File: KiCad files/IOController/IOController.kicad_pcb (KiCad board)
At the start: 2 copper layers, 30 x 74.3 mm, 48 parts, among them IC1 TPS922054DMTR, J1 AVR-ISP-6, J2 XT60 Horizontal Socket, J3 edge connector, Q1 BSS138, SW1 RotaryEncoder_Switch, SW2 TL3342, U1 LP2985-1.8, U3 LP2985-5.0, U4 ATtiny45V-10X

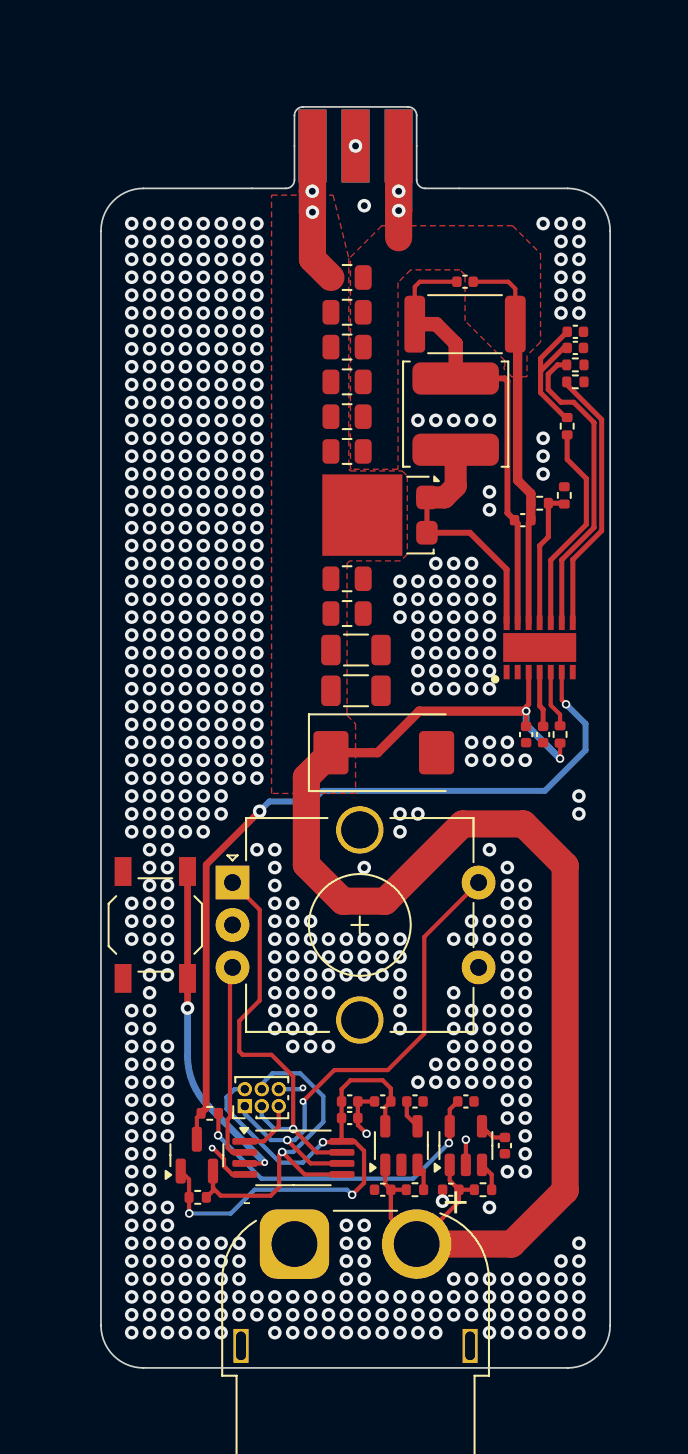
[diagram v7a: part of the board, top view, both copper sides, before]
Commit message: small adjustment to zones and added stitching vias
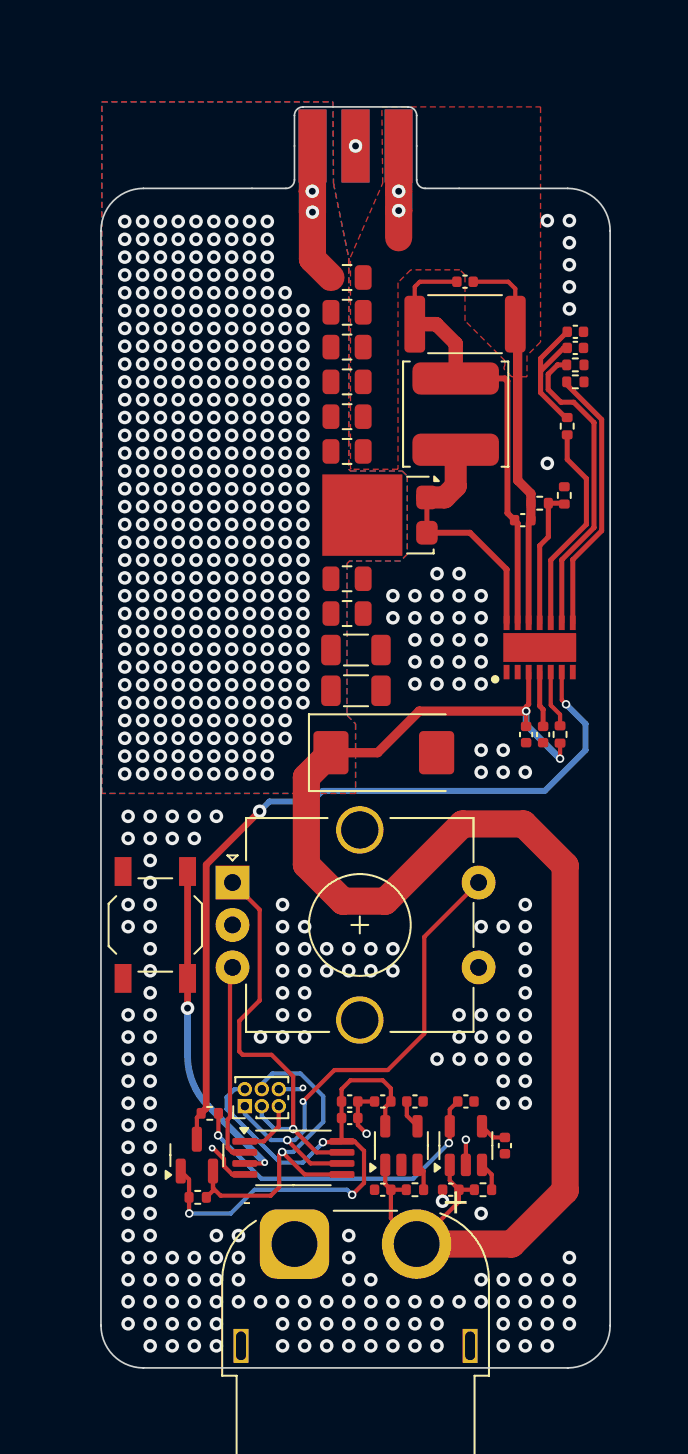
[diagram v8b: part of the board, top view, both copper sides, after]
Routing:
- net VCC: vias 4 -> 341
- net GND: vias 632 -> 205
- added copper zone on B.Cu, net VCC
